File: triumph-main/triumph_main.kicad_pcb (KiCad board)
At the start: 2 copper layers, 66 parts, among them J1 JST_XH_vert_01x04, J10 JST_XH_vert_01x04, J2 JST_PH_vert_01x03, J3 JST_PH_vert_01x03, J4 JST_PH_vert_01x06, J5 Conn_BNC, J6 JST_PH_vert_01x03, J7 JST_PH_vert_01x06, J8 JST_PH_vert_01x03, J9 JST_PH_vert_01x03, Q1 J310, U1 LM211P, U2 NE5532AP, U3 NE5532AP, U4 NE5532AP, U5 NE5532AP

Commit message: Continue placement
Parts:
- moved RV1 75.1 mm to (105.4, 52.1), turned to 90 degrees
- moved RV2 41.0 mm to (147.3, 59.7)
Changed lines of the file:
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@@
     (solder_mask_min_width 0.25)
     (aux_axis_origin 0 0)
-    (visible_elements FFFFFF7F)
+    (visible_elements 7FFFFFFF)
     (pcbplotparams
       (layerselection 0x010fc_ffffffff)
@@
   )
   (module Potentiometer_THT:Potentiometer_Bourns_3296W_Vertical (layer F.Cu)
-    (at 158.44 99.14)
+    (at 147.32 59.69)
     (descr "Potentiometer, vertical, Bourns 3296W, https://www.bourns.com/pdfs/3296.pdf")
     (tags "Potentiometer vertical Bourns 3296W")
@@
   )
   (module Potentiometer_THT:Potentiometer_Bourns_3296W_Vertical (layer F.Cu)
-    (at 139.79 118.79)
+    (at 105.41 52.07 90)
     (descr "Potentiometer, vertical, Bourns 3296W, https://www.bourns.com/pdfs/3296.pdf")
     (tags "Potentiometer vertical Bourns 3296W")
-    (fp_text reference RV1 (at -2.54 -3.66) (layer F.SilkS)
-      (effects (font (size 1 1) (thickness 0.15)))
-    )
-    (fp_text value 10K (at -2.54 3.67) (layer F.Fab)
-      (effects (font (size 1 1) (thickness 0.15)))
-    )
-    (fp_text user %R (at -3.175 0.005) (layer F.Fab)
+    (fp_text reference RV1 (at -2.54 -3.66 90) (layer F.SilkS)
+      (effects (font (size 1 1) (thickness 0.15)))
+    )
+    (fp_text value 10K (at -2.54 3.67 90) (layer F.Fab)
+      (effects (font (size 1 1) (thickness 0.15)))
+    )
+    (fp_text user %R (at -3.175 0.005 90) (layer F.Fab)
       (effects (font (size 1 1) (thickness 0.15)))
     )
@@
     (fp_line (start -7.305 -2.41) (end -7.305 2.42) (layer F.Fab) (width 0.1))
     (fp_circle (center 0.955 1.15) (end 2.05 1.15) (layer F.Fab) (width 0.1))
-    (pad 3 thru_hole circle (at -5.08 0) (size 1.44 1.44) (drill 0.8) (layers *.Cu *.Mask)
+    (pad 3 thru_hole circle (at -5.08 0 90) (size 1.44 1.44) (drill 0.8) (layers *.Cu *.Mask)
       (net 27 "Net-(R5-Pad1)"))
-    (pad 2 thru_hole circle (at -2.54 0) (size 1.44 1.44) (drill 0.8) (layers *.Cu *.Mask)
+    (pad 2 thru_hole circle (at -2.54 0 90) (size 1.44 1.44) (drill 0.8) (layers *.Cu *.Mask)
       (net 16 /FC_1))
-    (pad 1 thru_hole circle (at 0 0) (size 1.44 1.44) (drill 0.8) (layers *.Cu *.Mask)
+    (pad 1 thru_hole circle (at 0 0 90) (size 1.44 1.44) (drill 0.8) (layers *.Cu *.Mask)
       (net 16 /FC_1))
     (model ${KISYS3DMOD}/Potentiometer_THT.3dshapes/Potentiometer_Bourns_3296W_Vertical.wrl

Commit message: Continue placement
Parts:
- removed the C11 at (141.0, 68.6)
- removed the C18 at (163.8, 88.9)
- removed the C8 at (164.8, 116.3)
- added C10: 6.8uF, Capacitor_Tantalum_SMD:CP_EIA-3528-21_Kemet-B_Pad1.50x2.35mm_HandSolder, F.Cu at (148.2, 40.6)
- added C14: 1uF, triumph:0805_C_HandSoldering, B.Cu at (147.3, 44.5)
- added C15: 0.1uF, triumph:0805_C_HandSoldering, B.Cu at (139.7, 40.6)
- added C19: 0.1uF, triumph:0805_C_HandSoldering, B.Cu at (135.9, 78.7)
- added C21: 6.8uF, Capacitor_Tantalum_SMD:CP_EIA-3528-21_Kemet-B_Pad1.50x2.35mm_HandSolder, F.Cu at (171.0, 122.4)
- added C24: 6.8uF, Capacitor_Tantalum_SMD:CP_EIA-3528-21_Kemet-B_Pad1.50x2.35mm_HandSolder, F.Cu at (174.6, 115.9)
- added C25: 0.1uF, triumph:0805_C_HandSoldering, B.Cu at (176.5, 96.5)
- added C26: 0.1uF, triumph:0805_C_HandSoldering, B.Cu at (176.5, 104.2)
- added C4: 0.1uF, triumph:0805_C_HandSoldering, F.Cu at (121.0, 42.2)
- added C5: 1uF, triumph:0805_C_HandSoldering, F.Cu at (115.0, 42.2)
- added C6: 10nF, triumph:0805_C_HandSoldering, F.Cu at (125.0, 42.2)
- C13: value 6.8uF -> 1uF; footprint Capacitor_Tantalum_SMD:CP_EIA-3528-21_Kemet-B_Pad1.50x2.35mm_HandSolder -> triumph:0805_C_HandSoldering; moved to B.Cu
- C16: value 6.8uF -> 0.1uF; footprint Capacitor_Tantalum_SMD:CP_EIA-3528-21_Kemet-B_Pad1.50x2.35mm_HandSolder -> triumph:0805_C_HandSoldering; moved to B.Cu
- C17: value 0.1uF -> 0.01uF
- C18: renamed from C10; moved to B.Cu
- C3: footprint Capacitor_Tantalum_SMD:CP_EIA-3528-21_Kemet-B_Pad1.50x2.35mm_HandSolder -> triumph:0805_C_HandSoldering
- C7: value 1uF -> 10uF; footprint triumph:0805_C_HandSoldering -> Capacitor_THT:CP_Radial_D5.0mm_P2.00mm
- C8: renamed from C4; footprint Capacitor_Tantalum_SMD:CP_EIA-3528-21_Kemet-B_Pad1.50x2.35mm_HandSolder -> Capacitor_THT:CP_Radial_D5.0mm_P2.00mm
- C9: value 0.01uF -> 6.8uF; footprint triumph:0805_C_HandSoldering -> Capacitor_Tantalum_SMD:CP_EIA-3528-21_Kemet-B_Pad1.50x2.35mm_HandSolder
- D1, D2: footprint Diode_SMD:D_1206_3216Metric_Pad1.42x1.75mm_HandSolder -> triumph:D_SOD-123_HandSoldering
- R8, R9: moved to B.Cu
- moved C3 100.3 mm to (111.0, 42.2), turned to 90 degrees
- moved C18 96.2 mm to (147.4, 36.8)
- moved C9 95.9 mm to (138.1, 40.6)
- moved J2 92.4 mm to (96.5, 47.0), turned to 90 degrees
- moved R7 86.6 mm to (120.6, 55.9), turned to 180 degrees
- moved J7 85.8 mm to (113.0, 33.0), turned to 0 degrees
- moved R5 84.7 mm to (106.7, 63.5)
- moved R10 83.6 mm to (109.2, 59.7)
- moved C8 82.5 mm to (148.1, 48.3), turned to 180 degrees
- moved C7 79.8 mm to (139.0, 48.3)
- moved R4 79.2 mm to (104.1, 138.4), turned to 270 degrees
- moved R1 76.6 mm to (106.5, 82.0), turned to 180 degrees
- moved RV2 73.1 mm to (215.9, 85.1), turned to 180 degrees
- moved R17 72.1 mm to (143.5, 165.1)
- moved R2 71.9 mm to (106.5, 86.0), turned to 180 degrees
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- renumbered C5 to C11, C6 to C12, C12 to C20, C14 to C22, C15 to C23
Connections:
- C16 pad 1: -12V -> GND
- C16 pad 2: GND -> -12V
- C17 pad 1: GND -> +12V
- C17 pad 2: +12V -> GND
- C3 pad 1: +12V -> /SIG_TRI_RAW
- C3 pad 2: GND -> /FC_1
- J7 pad 2: /FC_1 -> /FC_2
- J7 pad 5: /FC_1 -> /FC_3
- J7 pad 6: /FC_1 -> /FC_4
- JP1 pad 1: /FC_1 -> /SIG_TRI_RAW
- R15 pad 1: /FC_1 -> /SIG_TRI_RAW
- RV1 pad 1: /FC_1 -> /SIG_TRI_RAW
- RV1 pad 2: /FC_1 -> /SIG_TRI_RAW
- RV2 pad 1: /FC_1 -> /SIG_TRI_RAW
- U1 pad 3: /FC_1 -> /SIG_TRI_RAW
- U2 pad 7: /FC_1 -> /SIG_TRI_RAW

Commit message: Continue placement
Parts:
- removed the C10 at (148.2, 40.6)
- removed the C16 at (147.3, 40.6)
- removed the C21 at (171.0, 122.4)
- removed the C24 at (174.6, 115.9)
- removed the C9 at (138.1, 40.6)
- added C12: 1uF, triumph:0805_C_HandSoldering, B.Cu at (147.4, 49.5)
- added C19: 10uF, triumph:0805_C_HandSoldering, B.Cu at (134.6, 96.5)
- added C22: 10uF, triumph:0805_C_HandSoldering, B.Cu at (119.4, 104.2)
- added C23: 10uF, triumph:0805_C_HandSoldering, B.Cu at (157.5, 96.5)
- added C26: 10uF, triumph:0805_C_HandSoldering, B.Cu at (142.2, 104.2)
- added REF**: MountingHole_3.2mm_M3_ISO14580_Pad, MountingHole:MountingHole_3.2mm_M3_ISO14580_Pad, F.Cu at (101.6, 111.8)
- added REF**: MountingHole_3.2mm_M3_ISO14580_Pad, MountingHole:MountingHole_3.2mm_M3_ISO14580_Pad, F.Cu at (177.8, 35.6)
- added REF**: MountingHole_3.2mm_M3_ISO14580_Pad, MountingHole:MountingHole_3.2mm_M3_ISO14580_Pad, F.Cu at (101.6, 35.6)
- C14: value 1uF -> 0.1uF
- R1, R2, R3, R4: moved to B.Cu
- moved R22 112.0 mm to (156.3, 43.2)
- moved J3 91.3 mm to (178.4, 45.6), turned to 270 degrees
- moved JP2 88.4 mm to (165.8, 78.7)
- moved R14 88.1 mm to (146.1, 68.4), turned to 0 degrees
- moved Q1 84.0 mm to (144.8, 59.5), turned to 270 degrees
- moved D2 83.2 mm to (152.4, 66.4), turned to 90 degrees
- moved R9 82.9 mm to (152.4, 65.8), turned to 270 degrees
- moved RV2 82.8 mm to (137.2, 59.5), turned to 90 degrees
- moved R13 81.7 mm to (146.0, 55.7), turned to 180 degrees
- moved R8 81.3 mm to (152.4, 58.3), turned to 270 degrees
- moved D1 81.1 mm to (152.4, 57.6), turned to 270 degrees
- moved RV3 77.5 mm to (129.5, 78.7), turned to 90 degrees
- moved R2 76.8 mm to (171.8, 45.6), turned to 0 degrees
- moved R17 75.5 mm to (127.0, 91.4)
- moved R1 72.9 mm to (171.8, 49.6), turned to 0 degrees
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- renumbered C12 to C10, C13 to C11, C15 to C13, C17 to C15, C18 to C16, C19 to C17, C20 to C18, C22 to C20, C23 to C21, C25 to C24, C26 to C25, C11 to C9
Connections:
- RV5 pad 1: /APL_1 -> /SIG_PREOUT
- RV5 pad 3: /SIG_PREOUT -> /APL_1
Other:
- board outline added: 86.4 x 86.4 mm

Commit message: Determine board edge
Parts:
- added REF**: MountingHole_3.2mm_M3_ISO14580_Pad, MountingHole:MountingHole_3.2mm_M3_ISO14580_Pad, F.Cu at (190.5, 137.2)
- moved REF** 28.4 mm to (190.5, 61.0)
- moved C1 25.4 mm to (166.4, 83.8)
- moved C10 25.4 mm to (121.9, 91.5)
- moved C11 25.4 mm to (139.7, 74.9)
- moved C12 25.4 mm to (147.4, 74.9)
- moved C17 25.4 mm to (143.5, 102.8)
- moved C19 25.4 mm to (134.6, 121.9)
- moved C2 25.4 mm to (166.4, 91.5)
- moved C20 25.4 mm to (127.0, 121.9)
- moved C21 25.4 mm to (127.0, 129.6)
- moved C22 25.4 mm to (119.4, 129.6)
- moved C23 25.4 mm to (157.5, 121.9)
- moved C24 25.4 mm to (149.9, 121.9)
- moved C25 25.4 mm to (149.9, 129.6)
- moved C26 25.4 mm to (142.2, 129.6)
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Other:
- board size 86.4 x 86.4 mm -> 99.1 x 86.4 mm

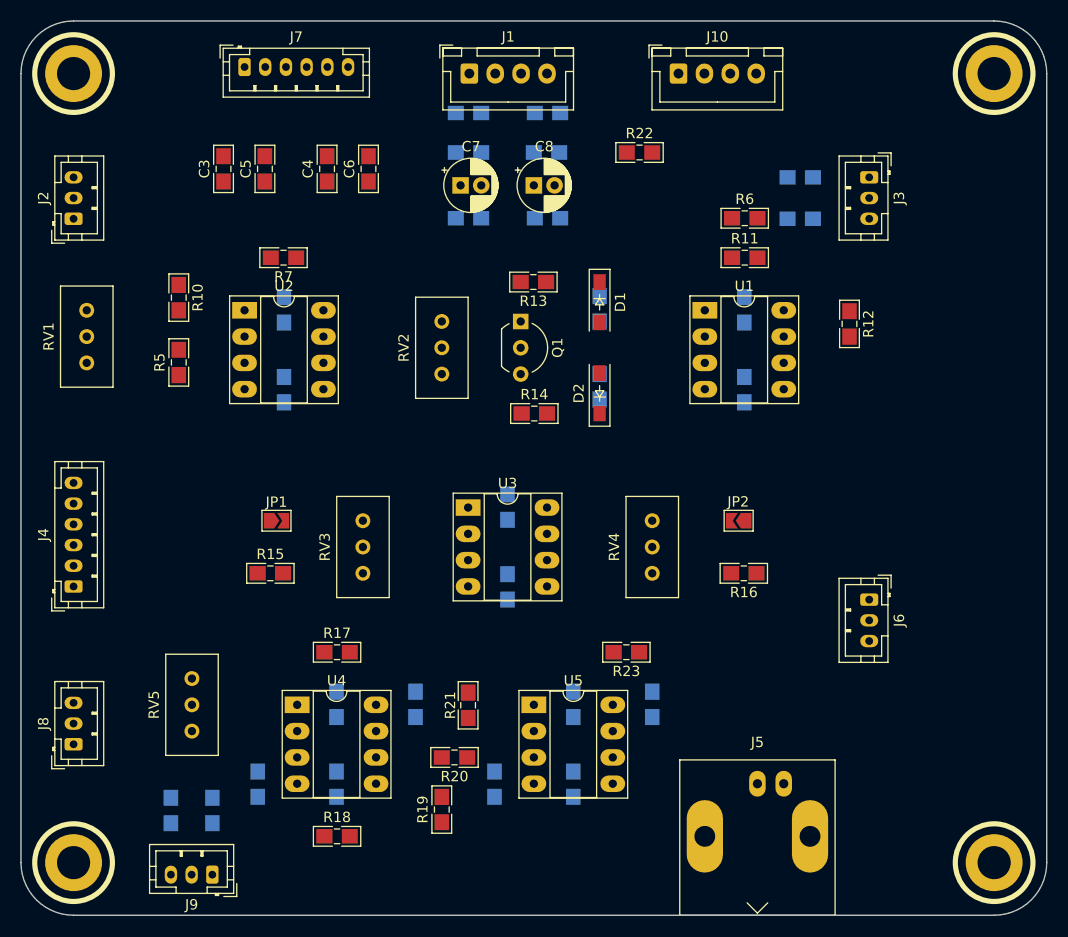
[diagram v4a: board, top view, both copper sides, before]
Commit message: Determine board outline
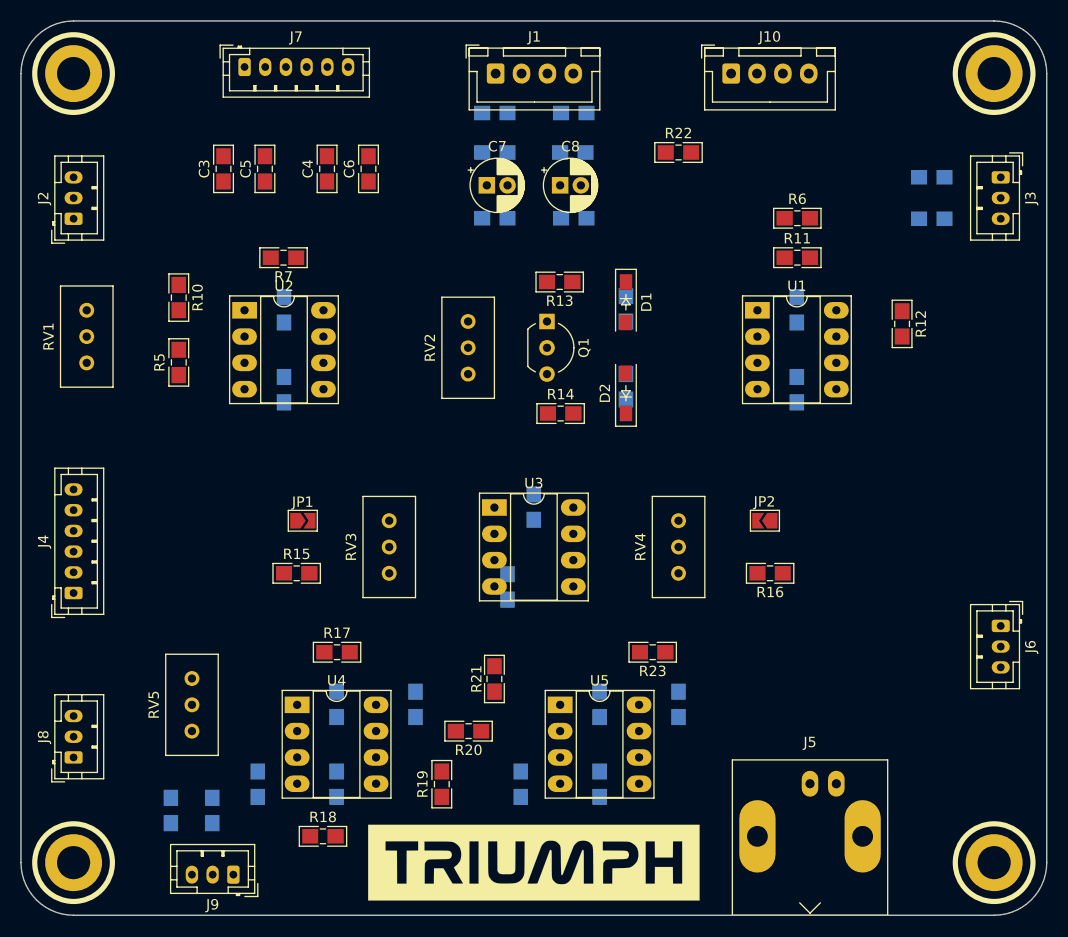
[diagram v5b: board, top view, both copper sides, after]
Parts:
- added G***: LOGO, triumph-logos:triumph-logo-inv, F.Cu at (146.1, 137.2)
- moved J6 13.0 mm to (191.1, 114.3)
- moved J3 12.7 mm to (191.1, 71.0)
- moved R1 12.7 mm to (184.5, 75.0)
- moved R2 12.7 mm to (184.5, 71.0)
- moved J5 5.08 mm to (172.7, 129.5)
- moved R11 5.08 mm to (171.5, 78.7)
- moved R12 5.08 mm to (181.6, 85.1)
- moved R6 5.08 mm to (171.5, 74.9)
- moved C1 5.08 mm to (171.4, 83.8)
- moved C2 5.08 mm to (171.4, 91.5)
- moved J10 5.08 mm to (165.1, 61.0)
- moved U1 5.08 mm to (167.6, 83.8)
- moved R22 3.77 mm to (160.0, 68.6)
- moved R21 3.59 mm to (142.2, 119.4)
- moved R20 2.88 mm to (139.7, 124.5)
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
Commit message: Begin routing
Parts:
- J5: footprint Connector_Coaxial:BNC_Amphenol_B6252HB-NPP3G-50_Horizontal -> triumph:Conn_BNC_73100-0154
- moved J5 13.0 mm to (175.3, 142.2)
- moved R23 10.8 mm to (165.1, 124.5)
- moved J6 8.79 mm to (192.4, 123.0)
- moved C18 2.84 mm to (146.1, 109.3)
- moved R22 2.29 mm to (158.1, 67.3)
- moved C12 2.29 mm to (149.8, 72.6)
- moved C11 2.29 mm to (142.3, 72.6)
- moved JP1 2.07 mm to (123.2, 102.1), turned to 270 degrees
- moved JP2 2.07 mm to (168.9, 102.1), turned to 270 degrees
- moved J4 2.01 mm to (99.7, 110.5)
- moved J2 1.91 mm to (99.7, 74.9)
- moved C7 1.91 mm to (141.5, 69.8)
- moved C8 1.91 mm to (148.6, 69.8)
- moved J8 1.91 mm to (99.7, 127.0)
- moved R18 1.80 mm to (124.4, 133.3)
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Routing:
- net /SIG_TRI_RAW: track 0.00 -> 116.5 mm
- net +12V: track 0.00 -> 116.4 mm, vias 0 -> 2
- net -12V: track 0.00 -> 103.8 mm, vias 0 -> 1
- net /SIG_SQR_RAW: track 0.00 -> 43.4 mm
- net /SIG_OUT: track 0.00 -> 39.4 mm
- net /APL_2: track 0.00 -> 31.4 mm
- net Net-(R17-Pad2): track 0.00 -> 31.4 mm
- net /APL_1: track 0.00 -> 28.8 mm
- net Net-(R21-Pad1): track 0.00 -> 26.8 mm
- net Net-(D1-Pad1): track 0.00 -> 26.2 mm, vias 0 -> 1
- net /FR_1: track 0.00 -> 25.7 mm
- net /SIG_SQR: track 0.00 -> 24.4 mm
- net /FR_2: track 0.00 -> 23.7 mm
- net Net-(J10-Pad1): track 0.00 -> 22.7 mm
- net /SIG_TRI: track 0.00 -> 22.6 mm
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- added copper zone on B.Cu, net GND
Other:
- net class Default: clearance 0.2 -> 0.1905; trace_width 0.25 -> 0.254; via_dia 0.8 -> 0.762; via_drill 0.4 -> 0.381
- net class Power added: clearance 0.1905, trace_width 0.762, via_dia 1.016, via_drill 0.48514
- net class Power-Thick added: clearance 0.1905, trace_width 1.27, via_dia 1.524, via_drill 0.762
- rule trace_clearance: 0.2 -> 0.1905
- board text added: "Function Generator Board Ray Sun EE 90"

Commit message: Add more cosmetics
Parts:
- added G***: LOGO, triumph-logos:caltech, F.Cu at (173.4, 121.9)
- added G***: LOGO, triumph-logos:rs, F.Cu at (182.0, 105.4)
- moved R23 2.54 mm to (165.1, 127.0)
- moved J6 0.25 mm to (192.4, 122.8)
- moved J8 0.25 mm to (99.7, 126.8)
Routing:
- net Net-(R21-Pad1): track 26.8 -> 27.7 mm
- net /SIG_OUT: track 39.4 -> 38.6 mm
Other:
- board text added: "+12V"
- board text added: "-12V"
- board text added: "GND"
- board text added: "LED+"
- board text added: "LED-"
- board text added: "SIG"

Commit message: Finish routing
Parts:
- moved C6 4.35 mm to (125.7, 69.5)
- moved C4 4.16 mm to (121.9, 69.5)
- moved C3 1.91 mm to (114.2, 69.5)
- moved C5 1.91 mm to (118.2, 69.5)
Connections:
- J4 pad 1: /SIG_SIN -> /SIG_PREOUT
- J4 pad 2: /SIG_SQR -> /SIG_PREOUT
- J4 pad 3: /SIG_PREOUT -> /SIG_SQR
- J4 pad 4: /SIG_PREOUT -> /SIG_TRI
- J4 pad 5: /SIG_TRI -> /SIG_SIN
- J7 pad 3: /FC_COM -> /FC_3
- J7 pad 4: /FC_COM -> /FC_4
- J7 pad 5: /FC_3 -> /FC_COM
- J7 pad 6: /FC_4 -> /FC_COM
- R3 pad 1: -12V -> +12V
- R4 pad 1: +12V -> -12V
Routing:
- net +12V: track 116.4 -> 268.4 mm, vias 2 -> 4
- net -12V: track 103.8 -> 247.7 mm, vias 1 -> 4
- net GND: track 5.08 -> 98.3 mm
- net /SIG_SQR: track 24.4 -> 78.4 mm
- net /SIG_SIN: track 8.57 -> 61.7 mm
- net /SIG_TRI_RAW: track 116.5 -> 164.8 mm, vias 0 -> 1
- net /FC_COM: track 14.5 -> 47.9 mm, vias 0 -> 2
- net /SIG_TRI: track 22.6 -> 46.8 mm, vias 0 -> 2
- net /SIG_PREOUT: track 0.00 -> 18.4 mm
- net Net-(R15-Pad2): track 7.71 -> 19.4 mm
- net /FC_1: track 0.00 -> 10.9 mm
- net /FC_2: track 0.00 -> 10.1 mm
- net /FC_4: track 0.00 -> 9.92 mm
- net /FC_3: track 0.00 -> 9.33 mm
- net /SIG_SQR_RAW: track 43.4 -> 48.9 mm
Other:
- board text added: "AMPLT"
- board text added: "DC"
- board text added: "FREQ"
- board text added: "FREQ SEL"
- board text added: "OFFSET"
- board text added: "OUT"
- board text added: "OUTPUT SEL"
- board text added: "SIN"
- board text added: "SQR"
- board text added: "TRI"
